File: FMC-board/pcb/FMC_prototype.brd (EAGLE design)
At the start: 76.5 x 69 mm, 108 parts, among them Q1 SSM3J328R, U1 4901, U2 7933, U3 ADN4663, U4 ADN4663, U5 ADN4664, U6 PDS1, U7 4901, U8 FMC_SINGLE_WIDTH_MODULE

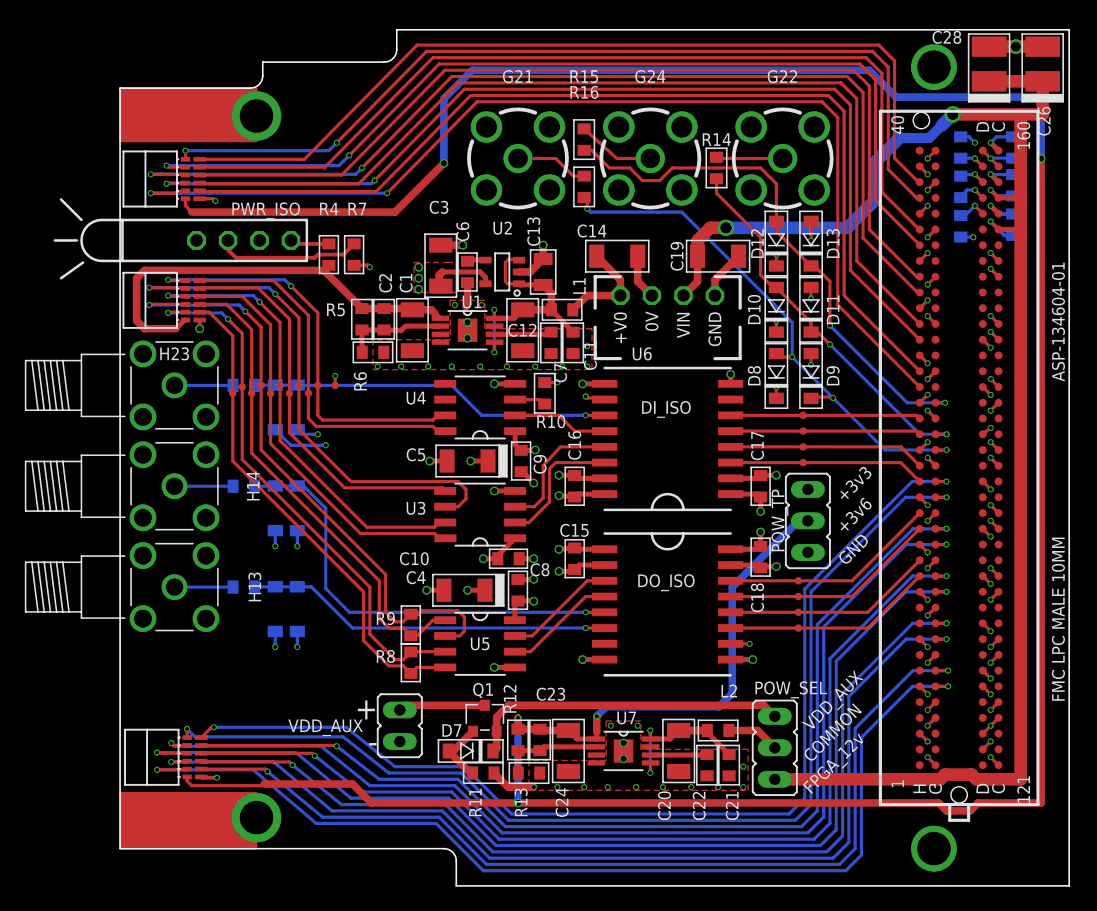
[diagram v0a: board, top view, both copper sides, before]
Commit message: Final, minor changes to sinkscreen and tp's
- Added isolated power test points
- Moved Jakobs annotations to the tplace and bplace layers, so that they
  will be included in the silkscreen using the CAM job I added
- Added a well-tested CAM job for 4-layer boards
- Added resultant gerber files for PCB and stencil
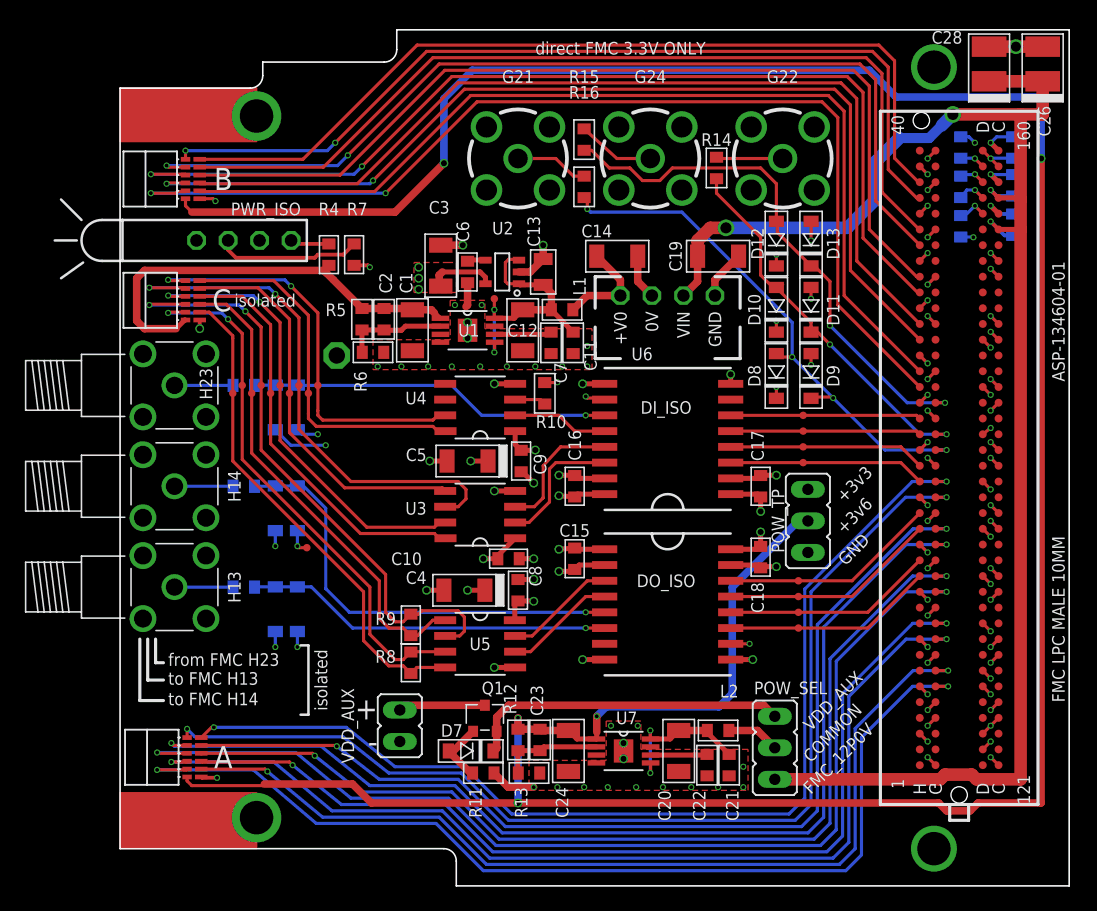
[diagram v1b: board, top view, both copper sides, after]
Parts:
- removed TP8: MOSI-, jonnew:TP06R
- added TP13: +3V3, jonnew:TP06R
- added TP14: MISO1-, jonnew:TP06R
- added TP15: +5V0, jonnew:TP06R
- added TP2: MOSI+, jonnew:TP06R
- TP1: device jonnew:TP06R -> jonnew:P1-13
- TP10: value SCLK- -> +3V6
- TP11: value CS+ -> MISO2-
- TP12: value CS- -> MISO1+
- TP3: value MISO2+ -> SCLK+
- TP4: value MISO2- -> CS-
- TP5: value MISO1+ -> MOSI-
- TP6: value MISO1- -> SCLK-
- TP7: value MOSI+ -> CS+
- TP9: value SCLK+ -> MISO2+
- moved TP10 9.81 mm to (-48.4, 45.8), turned to 0 degrees
- moved TP11 6.89 mm to (-56.5, 36.7), turned to 90 degrees
- moved TP4 6.10 mm to (-50.4, 36.7)
- moved TP3 4.57 mm to (-51.2, 37.3)
- moved TP9 4.57 mm to (-55.8, 37.3)
- moved TP12 3.86 mm to (-54.2, 37.3), turned to 270 degrees
- moved TP6 3.05 mm to (-51.9, 36.7)
- moved TP7 3.05 mm to (-49.7, 37.3)
- moved TP1 2.42 mm to (-48.1, 39.8)
- moved TP5 0.99 mm to (-53.5, 36.7), turned to 90 degrees
- renumbered TP_H13 to TP_H3, TP_H14 to TP_H2, TP_H23 to TP_H1, U$3 to U$1
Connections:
- removed net +5V0_ISO: C11.1, C12.1, C13.1, L1.2, U1.5, U1.8, U2.1, U2.3
- new net +5V0: C11.1, C12.1, C13.1, L1.2, TP15.TP, U1.5, U1.8, U2.1, U2.3
- net +3V3_ISO: now also TP13.TP
- net +3V6_ISO: now also TP10.TP
- net CS+_ISOLATED: now also TP7.TP; no longer TP11.TP
- net CS-_ISOLATED: now also TP4.TP; no longer TP12.TP
- net MISO1+_ISOLATED: now also TP12.TP; no longer TP5.TP
- net MISO1-_ISOLATED: now also TP14.TP; no longer TP6.TP
- net MISO2+_ISOLATED: now also TP9.TP; no longer TP3.TP
- net MISO2-_ISOLATED: now also TP11.TP; no longer TP4.TP
- net N$12: now also TP2.TP; no longer TP7.TP
- net N$13: now also TP5.TP; no longer TP8.TP
- net N$15: now also TP3.TP; no longer TP9.TP
- net N$16: now also TP6.TP; no longer TP10.TP
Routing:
- net +5V0: track 0.00 -> 21.4 mm, vias 0 -> 2
- net +5V0_ISO: track 20.5 -> 0.00 mm, vias 2 -> 0
- net +3V6_ISO: track 34.9 -> 36.0 mm
- net +3V3_ISO: track 32.9 -> 33.7 mm
- net GND_ISO: track 43.4 -> 42.6 mm, vias 34 -> 33
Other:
- board text added: "FMC_12P0V"
- board text added: "G21"
- board text added: "G22"
- board text added: "G24"
- board text added: "direct FMC 3.3V ONLY"
- board text added: "from FMC H23"
- board text added: "to FMC H13"
- board text added: "to FMC H14"
- board text removed: "FPGA_12v"
- board text removed: "direct_fpga 3.3V ONLY"
- board text removed: "direct_fpga_G21"
- board text removed: "direct_fpga_G22"
- board text removed: "direct_fpga_H1G24 3.3V ONLY"
- board text removed: "from_fpga_H23"
- board text removed: "to_fpga_H13"
- board text removed: "to_fpga_H14"
